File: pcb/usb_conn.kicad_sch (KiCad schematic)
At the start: 33 parts, among them J2 CONN_USBC_RCPT_USB2.0_USB4085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, Q2 NFET_60V_0A5_2N7002KT1G, U8 IC_FTDI_FT231XS, U9 IC_LSW_TI_TPS2552D

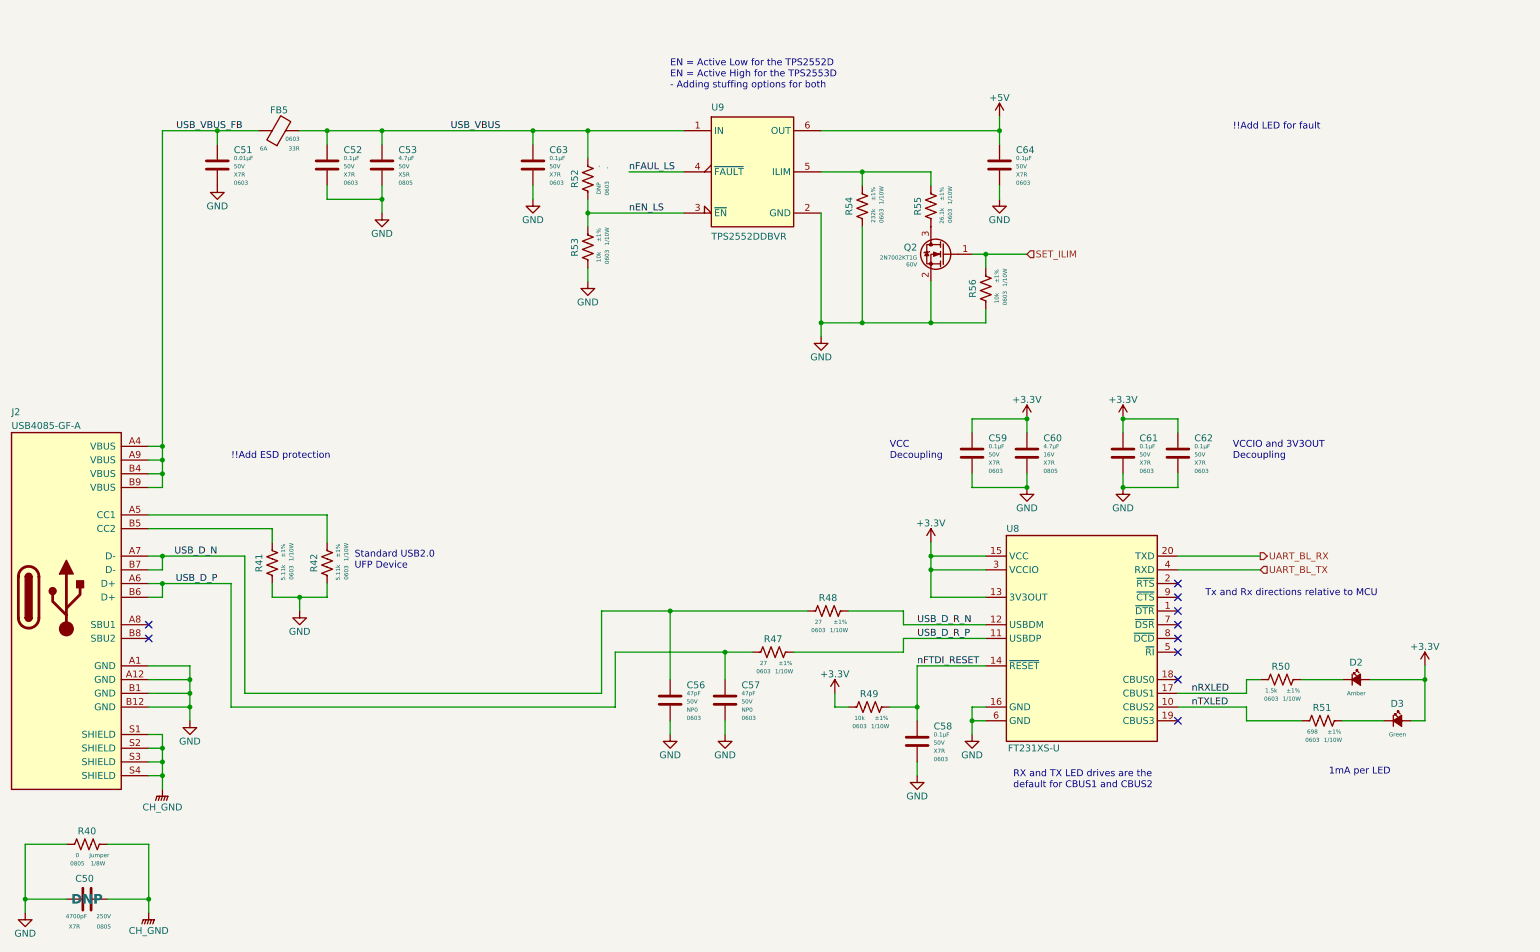
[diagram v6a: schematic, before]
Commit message: Added load switch fault LED and some notes on usb esd diodes
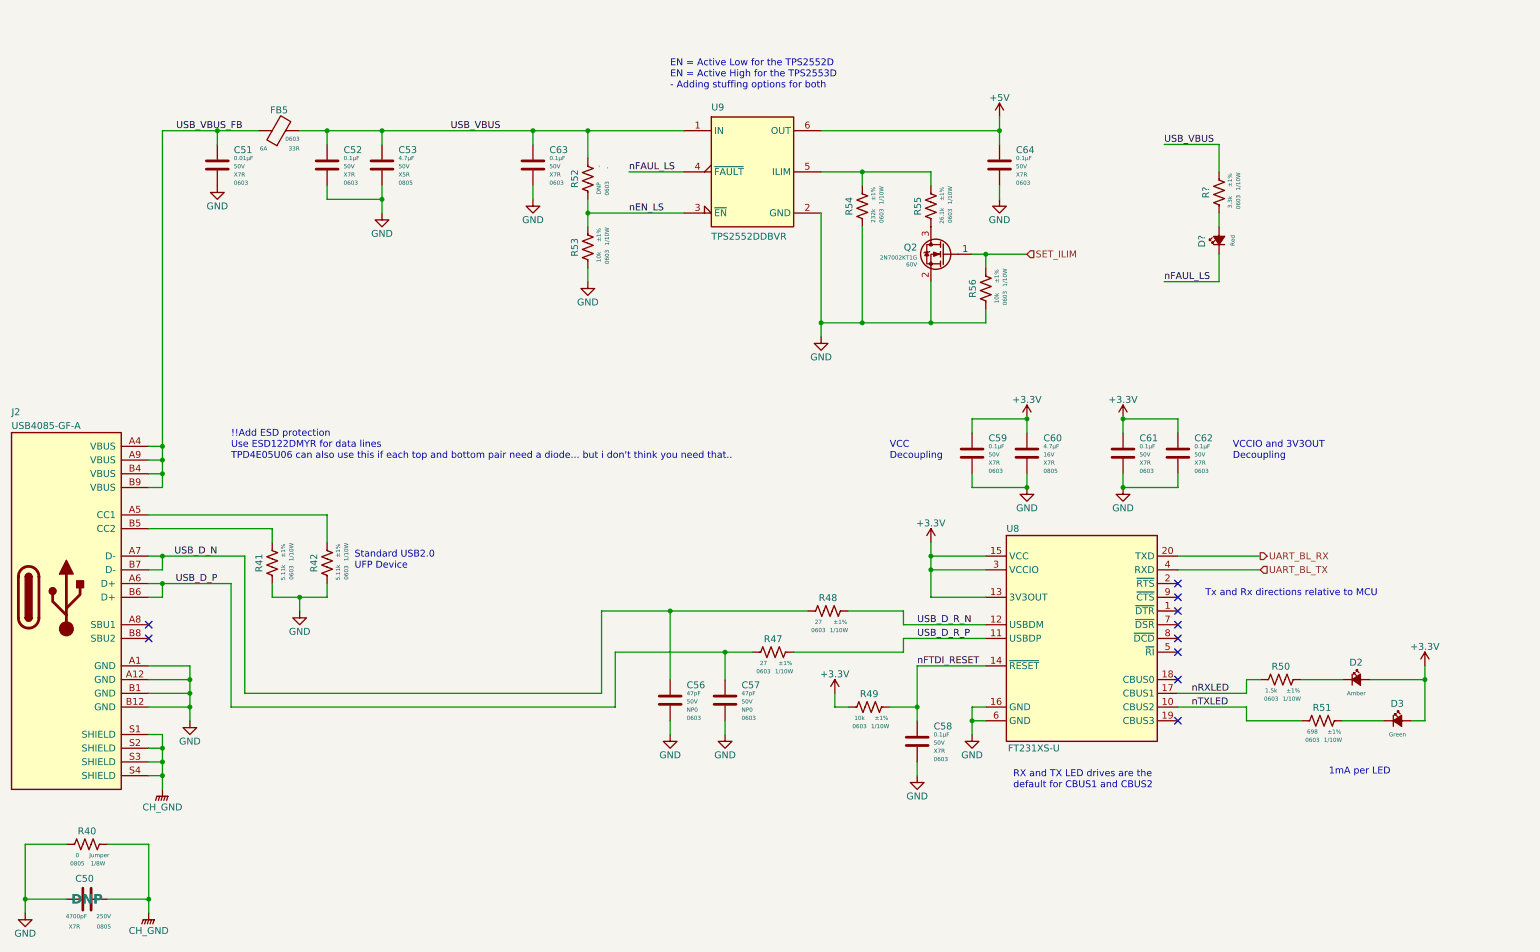
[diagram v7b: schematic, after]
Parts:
- added D?: LED_RED_0603, LED_SMD:LED_0603_1608Metric, symbol .arjun:LED_RED_0603
- added R?: RES_3K3_1P_1/10W_0603, Resistor_SMD:R_0603_1608Metric, symbol .arjun:RES_3K3_1P_1/10W_0603
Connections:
- net USB_VBUS: now also R?.1
- net nFAUL_LS: now also D?.1 (K)
- new net: D?.2 (A), R?.2
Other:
- note added: "!!Add ESD protection Use ESD122DMYR for data lines TPD4E05U06 can also use this if each top and bottom pair need a diode... but i don't think you need that.."
- note removed: "!!Add ESD protection"
- note removed: "!!Add LED for fault"
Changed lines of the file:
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@@
+    (stroke (width 0) (type default) (color 0 0 0 0))
+  )
+  (wire (pts (xy 241.3 58.42) (xy 241.3 63.5))
     (stroke (width 0) (type default) (color 0 0 0 0))
   )
@@
     (stroke (width 0) (type default) (color 0 0 0 0))
   )
+  (wire (pts (xy 231.14 63.5) (xy 241.3 63.5))
+    (stroke (width 0) (type default) (color 0 0 0 0))
+  )
   (wire (pts (xy 182.88 127) (xy 198.12 127))
     (stroke (width 0) (type default) (color 0 0 0 0))
@@
     (stroke (width 0) (type default) (color 0 0 0 0))
   )
+  (wire (pts (xy 241.3 43.18) (xy 241.3 38.1))
+    (stroke (width 0) (type default) (color 0 0 0 0))
+  )
   (wire (pts (xy 50.8 139.7) (xy 50.8 142.24))
     (stroke (width 0) (type default) (color 0 0 0 0))
@@
     (stroke (width 0) (type default) (color 0 0 0 0))
   )
+  (wire (pts (xy 231.14 38.1) (xy 241.3 38.1))
+    (stroke (width 0) (type default) (color 0 0 0 0))
+  )
   (wire (pts (xy 43.18 134.62) (xy 50.8 134.62))
     (stroke (width 0) (type default) (color 0 0 0 0))
@@
   )
   (wire (pts (xy 185.42 142.24) (xy 185.42 144.78))
+    (stroke (width 0) (type default) (color 0 0 0 0))
+  )
+  (wire (pts (xy 241.3 50.8) (xy 241.3 53.34))
     (stroke (width 0) (type default) (color 0 0 0 0))
   )
@@
     (effects (font (size 1.27 1.27)) (justify left bottom))
   )
-  (text "!!Add LED for fault" (at 243.84 35.56 0)
-    (effects (font (size 1.27 1.27)) (justify left bottom))
-  )
   (text "EN = Active Low for the TPS2552D\nEN = Active High for the TPS2553D\n- Adding stuffing options for both"
     (at 139.7 27.94 0)
@@
     (effects (font (size 1.27 1.27)) (justify left bottom))
   )
-  (text "!!Add ESD protection" (at 58.42 96.52 0)
+  (text "!!Add ESD protection\nUse ESD122DMYR for data lines\nTPD4E05U06 can also use this if each top and bottom pair need a diode... but i don't think you need that.."
+    (at 58.42 96.52 0)
     (effects (font (size 1.27 1.27)) (justify left bottom))
   )
@@
     (effects (font (size 1.27 1.27)) (justify left bottom))
   )
+  (label "nFAUL_LS" (at 231.14 63.5 0)
+    (effects (font (size 1.27 1.27)) (justify left bottom))
+  )
   (label "USB_VBUS_FB" (at 48.26 35.56 0)
     (effects (font (size 1.27 1.27)) (justify left bottom))
@@
   )
   (label "nRXLED" (at 236.22 139.7 0)
+    (effects (font (size 1.27 1.27)) (justify left bottom))
+  )
+  (label "USB_VBUS" (at 231.14 38.1 0)
     (effects (font (size 1.27 1.27)) (justify left bottom))
   )
@@
     )
     (pin "1")
+  )
+  (symbol (lib_id ".arjun:LED_RED_0603") (at 241.3 55.88 90) (unit 1)
+    (in_bom yes) (on_board yes)
+    (property "Reference" "D?" (id 0) (at 238.125 57.15 0)
+      (effects (font (size 1.27 1.27)) (justify left))
+    )
+    (property "Value" "LED_RED_0603" (id 1) (at 231.14 43.18 0)
+      (effects (font (size 1.27 1.27)) (justify left) hide)
+    )
+    (property "Footprint" "LED_SMD:LED_0603_1608Metric" (id 2) (at 248.92 43.18 0)
+      (effects (font (size 1.27 1.27)) (justify left) hide)
+    )
+    (property "Datasheet" "https://www.we-online.com/components/products/datasheet/150060RS75000.pdf" (id 3) (at 246.38 43.18 0)
+      (effects (font (size 1.27 1.27)) (justify left) hide)
+    )
+    (property "Vendor" "Digi-Key" (id 4) (at 241.3 43.18 0)
+      (effects (font (size 1.27 1.27)) (justify left) hide)
+    )
+    (property "VendorPN" "732-4978-1-ND" (id 5) (at 243.84 43.18 0)
+      (effects (font (size 1.27 1.27)) (justify left) hide)
+    )
+    (property "Manufacturer" "Würth Elektronik" (id 6) (at 236.22 43.18 0)
+      (effects (font (size 1.27 1.27)) (justify left) hide)
+    )
+    (property "ManufacturerPN" "150060RS75000" (id 7) (at 238.76 43.18 0)
+      (effects (font (size 1.27 1.27)) (justify left) hide)
+    )
+    (property "Colour" "Red" (id 8) (at 243.84 55.88 0)
+      (effects (font (size 0.762 0.762)))
+    )
+    (property "Vf" "2V" (id 9) (at 233.68 43.18 0)
+      (effects (font (size 1.27 1.27)) (justify left) hide)
+    )
+    (pin "1")
+    (pin "2")
   )
   (symbol (lib_id "power:GND") (at 185.42 154.94 0) (unit 1)
@@
     (pin "S4")
   )
+  (symbol (lib_id ".arjun:RES_3K3_1P_1{slash}10W_0603") (at 241.3 43.18 0) (unit 1)
+    (in_bom yes) (on_board yes)
+    (property "Reference" "R?" (id 0) (at 238.125 46.99 90)
+      (effects (font (size 1.27 1.27)) (justify top))
+    )
+    (property "Value" "RES_3K3_1P_1/10W_0603" (id 1) (at 248.92 38.1 0)
+      (effects (font (size 1.27 1.27)) (justify left) hide)
+    )
+    (property "Footprint" "Resistor_SMD:R_0603_1608Metric" (id 2) (at 248.92 40.64 0)
+      (effects (font (size 1.27 1.27)) (justify left) hide)
+    )
+    (property "Datasheet" "https://www.seielect.com/catalog/sei-rmcf_rmcp.pdf" (id 3) (at 248.92 50.8 0)
+      (effects (font (size 1.27 1.27)) (justify left) hide)
+    )
+    (property "Manufacturer" "Stackpole Electronics Inc" (id 4) (at 248.92 45.72 0)
+      (effects (font (size 1.27 1.27)) (justify left) hide)
+    )
+    (property "ManufacturerPN" "RMCF0603FT3K30" (id 5) (at 248.92 48.26 0)
+      (effects (font (size 1.27 1.27)) (justify left) hide)
+    )
+    (property "Vendor" "Digi-Key" (id 6) (at 248.92 53.34 0)
+      (effects (font (size 1.27 1.27)) (justify left) hide)
+    )
+    (property "VendorPN" "RMCF0603FT3K30CT-ND" (id 7) (at 248.92 55.88 0)
+      (effects (font (size 1.27 1.27)) (justify left) hide)
+    )
+    (property "Resistance" "3.3k" (id 8) (at 243.332 48.768 90)
+      (effects (font (size 0.762 0.762)))
+    )
+    (property "Tolerance" "±1% " (id 9) (at 243.332 44.704 90)
+      (effects (font (size 0.762 0.762)))
+    )
+    (property "Package" "0603" (id 10) (at 244.856 48.768 90)
+      (effects (font (size 0.762 0.762)))
+    )
+    (property "Power" "1/10W" (id 11) (at 244.856 44.958 90)
+      (effects (font (size 0.762 0.762)))
+    )
+    (pin "1")
+    (pin "2")
+  )
   (symbol (lib_id "power:GND") (at 139.7 147.32 0) (unit 1)

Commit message: Added ESD protection to 5V input, leds, hw rev pins, and test points.
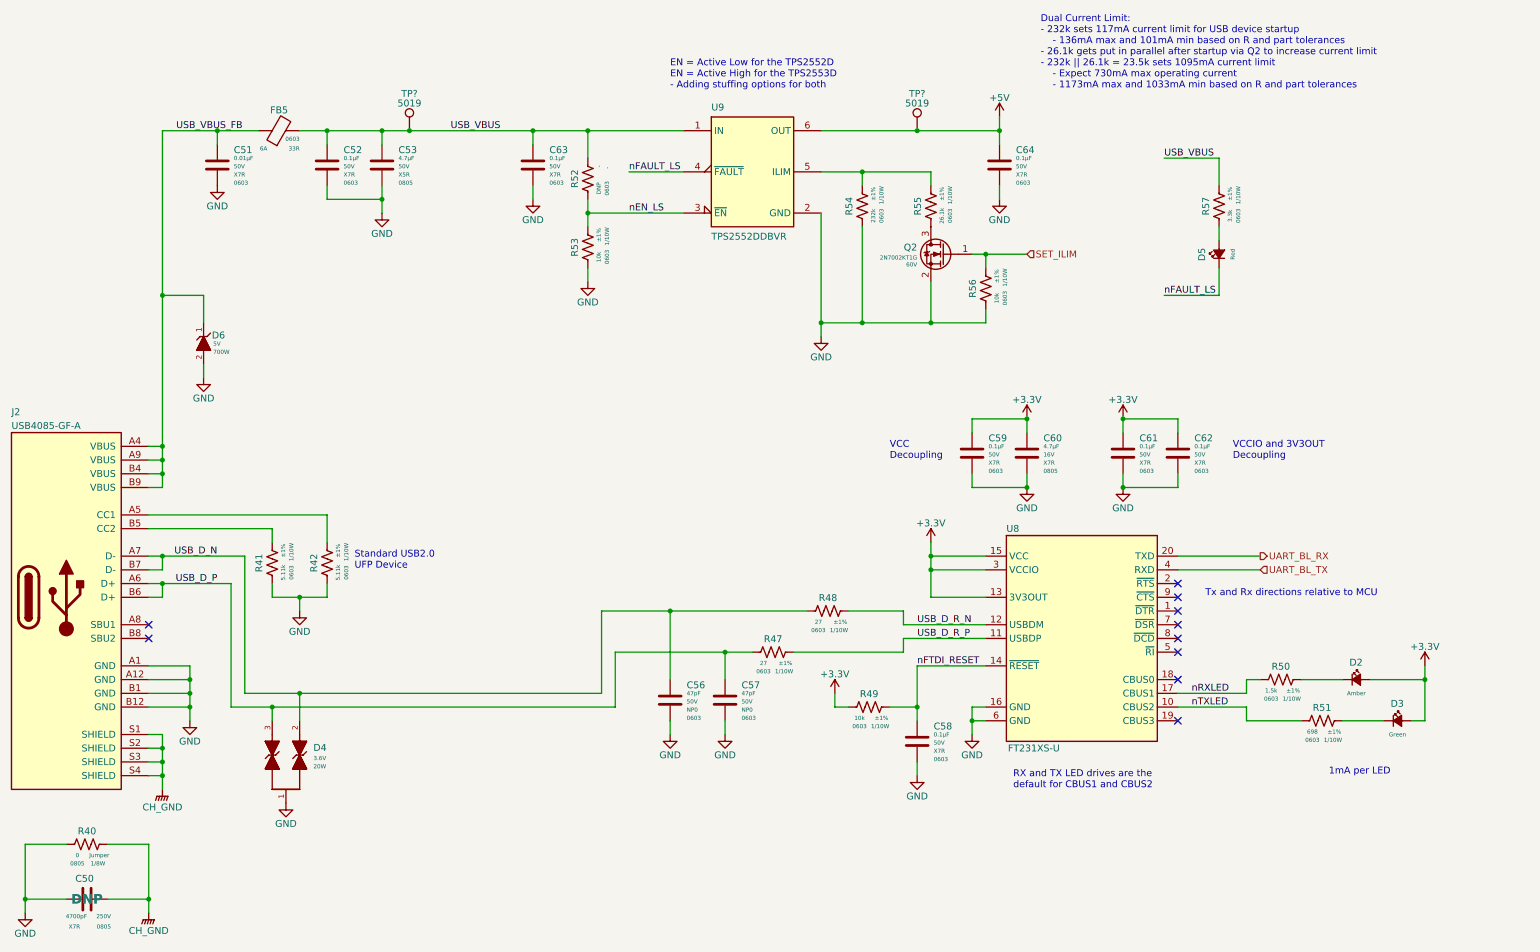
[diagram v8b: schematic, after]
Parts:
- added D4: D_TVS_BI_3V6_20W_3-XFDFN, arjun_footprints:DIO_ESD122DMYR, symbol .arjun:D_TVS_BI_3V6_20W_3-XFDFN
- added D6: D_TVS_UNI_5V_700W_2-UDFN, arjun_footprints:QFN-2L_STM, symbol .arjun:D_TVS_UNI_5V_700W_2-UDFN
- added TP? (x2): TP_KEYSTONE_5019, arjun_footprints:TestPoint_Keystone_5019_Minature, symbol .arjun:TP_KEYSTONE_5019
- gave numbers to parts that had none: 2
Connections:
- net +5V: now also TP?.1
- net GND: now also D4.1, D6.2 (A)
- net USB_D_N: now also D4.2
- net USB_D_P: now also D4.3
- net USB_VBUS: now also TP?.1
- net USB_VBUS_FB: now also D6.1 (K)
- net nFAUL_LS renamed nFAULT_LS
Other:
- note added: "Dual Current Limit: - 232k sets 117mA current limit for USB device startup - 136mA max and 101mA min based on R and part tolerances - 26.1k gets put in parallel after startup via Q2 to increase current limit - 232k || 26.1k = 23.5k sets 1095mA current limit - Expect 730mA max operating current - 1173mA max and 1033mA min based on R and part tolerances"
- note removed: "!!Add ESD protection Use ESD122DMYR for data lines TPD4E05U06 can also use this if each top and bottom pair need a diode... but i don't think you need that.."
- moved on the sheet: D5, R57
